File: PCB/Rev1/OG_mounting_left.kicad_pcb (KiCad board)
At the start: 2 copper layers, 133.8 x 91.4 mm, 54 parts, among them J1 OLED, J2 MJ-4PP-9, Q1 Q_NMOS_GSD, SW1 SW_Push, SW10 EC_SW, SW11 EC_SW, SW12 EC_SW, SW13 EC_SW, SW14 EC_SW, SW15 EC_SW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

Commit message: Fix pad numbering
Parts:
- renumbered SWe to SW7, SWe to SW9
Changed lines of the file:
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@@
     (property "Sheetname" "")
     (attr smd)
-    (fp_text reference "SWe" (at -6 -8) (layer "F.SilkS") hide
+    (fp_text reference "SW9" (at -6 -8) (layer "F.SilkS") hide
       (effects (font (size 0.8 0.8) (thickness 0.12)))
     )
@@
     (property "Sheetname" "")
     (attr smd)
-    (fp_text reference "SWe" (at -6 -8) (layer "F.SilkS") hide
-      (effects (font (size 0.8 0.8) (thickness 0.12)))
-    )
+    (fp_text reference "SW7" (at -6 -8) (layer "F.SilkS") hide
+      (effects (font (size 0.8 0.8) (thickness 0.12)))
+    )

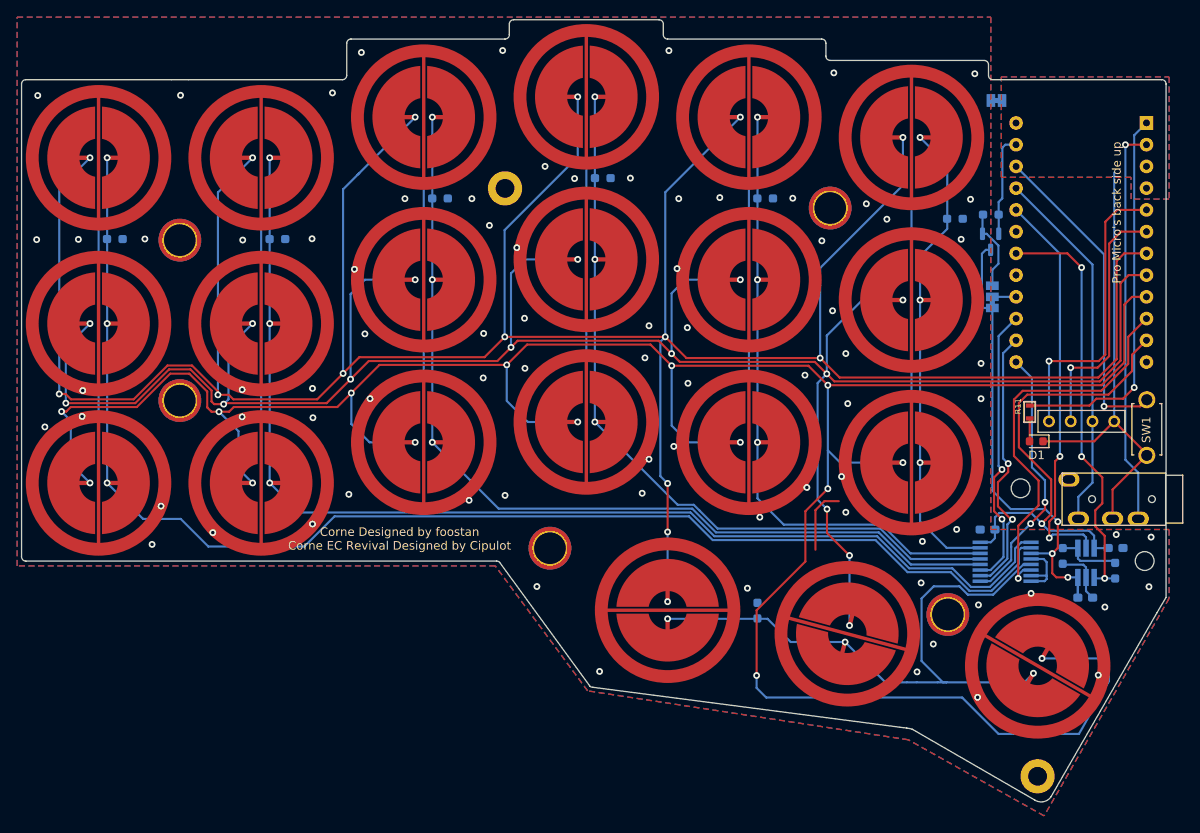
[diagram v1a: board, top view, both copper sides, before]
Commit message: FIX Production files
Fix to the production files that caused one of the 2 EC pads to be merged with the ground plane.
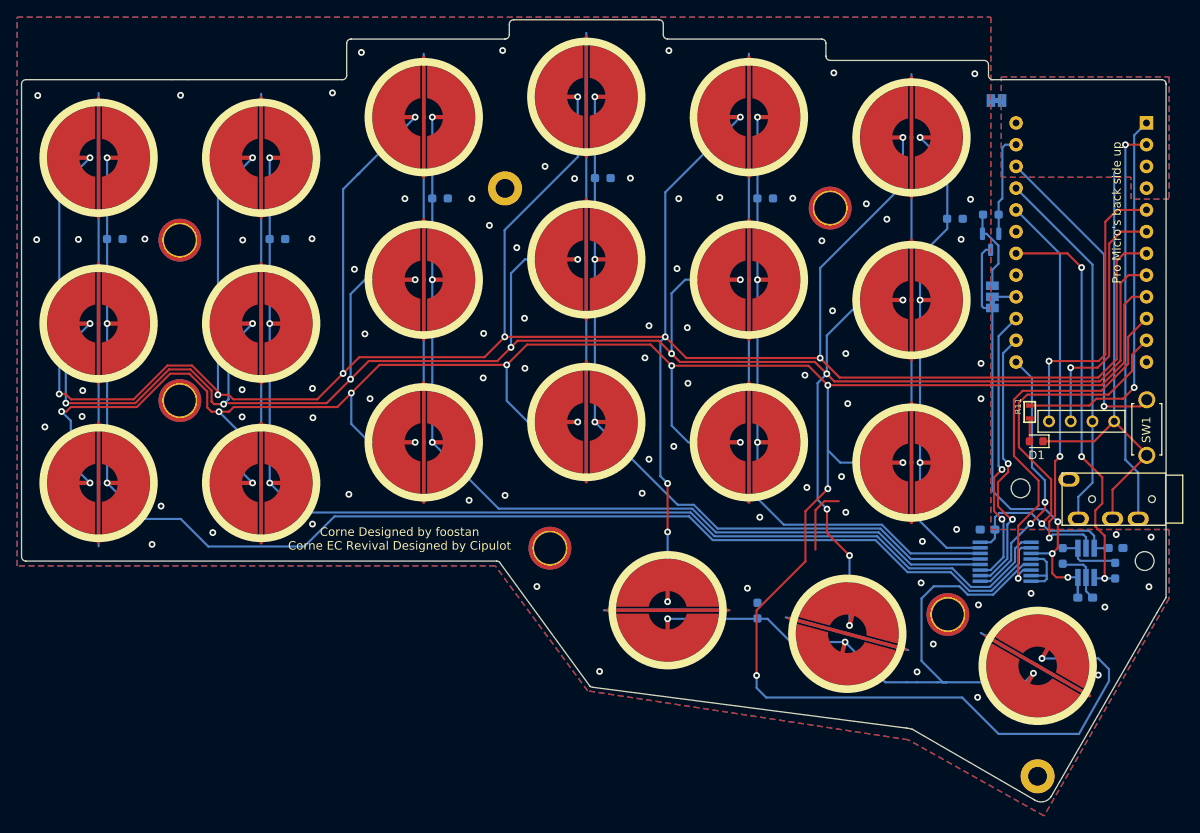
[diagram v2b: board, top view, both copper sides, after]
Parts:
- SW10, SW11, SW12, SW13, SW14, SW15, SW16, SW17, SW18, SW19, SW2, SW20, SW21, SW22, SW3, SW4, SW5, SW6, SW7, SW8, SW9: footprint cipulot_parts:ecs_pad -> cipulot_parts:ecs_pad_no_ring
